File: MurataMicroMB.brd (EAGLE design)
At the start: 90 x 63 mm, 47 parts, among them CON1 C-2395.MurataMicroSD, CON3 CON_MIL_10_ARM, CON4 C-2395.microSD, IC1 74LVC1G00DBV, IC2 IC_DCDC_LM27313, IC3 IC_LPC11U3XQFN33, IC4 IC_LDO_XX1117_4, Q1 CLOCK_CRYSTAL_4_3225, SW1 SW_TACTSW_2PP8073, SW2 SW_TACTSW_2PP8073, SW3 SW_TACTSW_2PP8073, X1 TSW-102-02-S-S

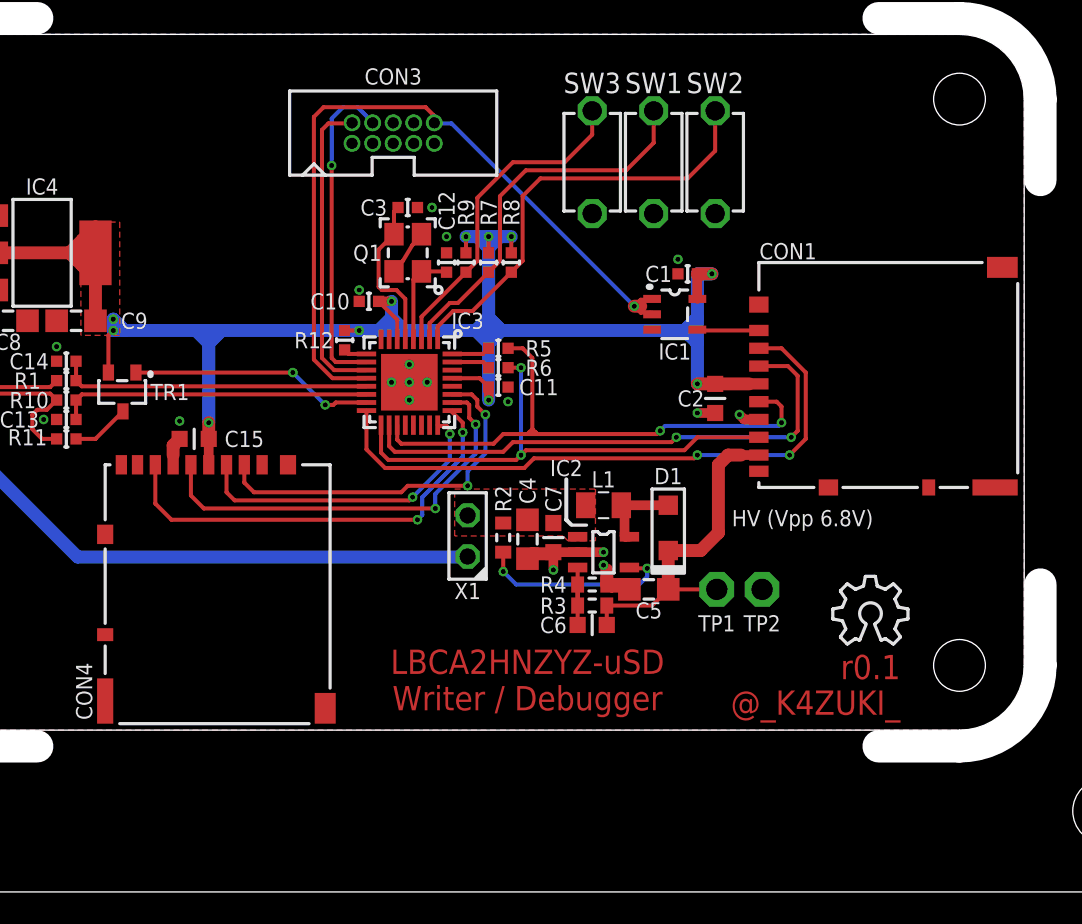
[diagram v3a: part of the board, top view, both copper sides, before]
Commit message: [ MB ][ SCH ] connection to uSD sockets changed
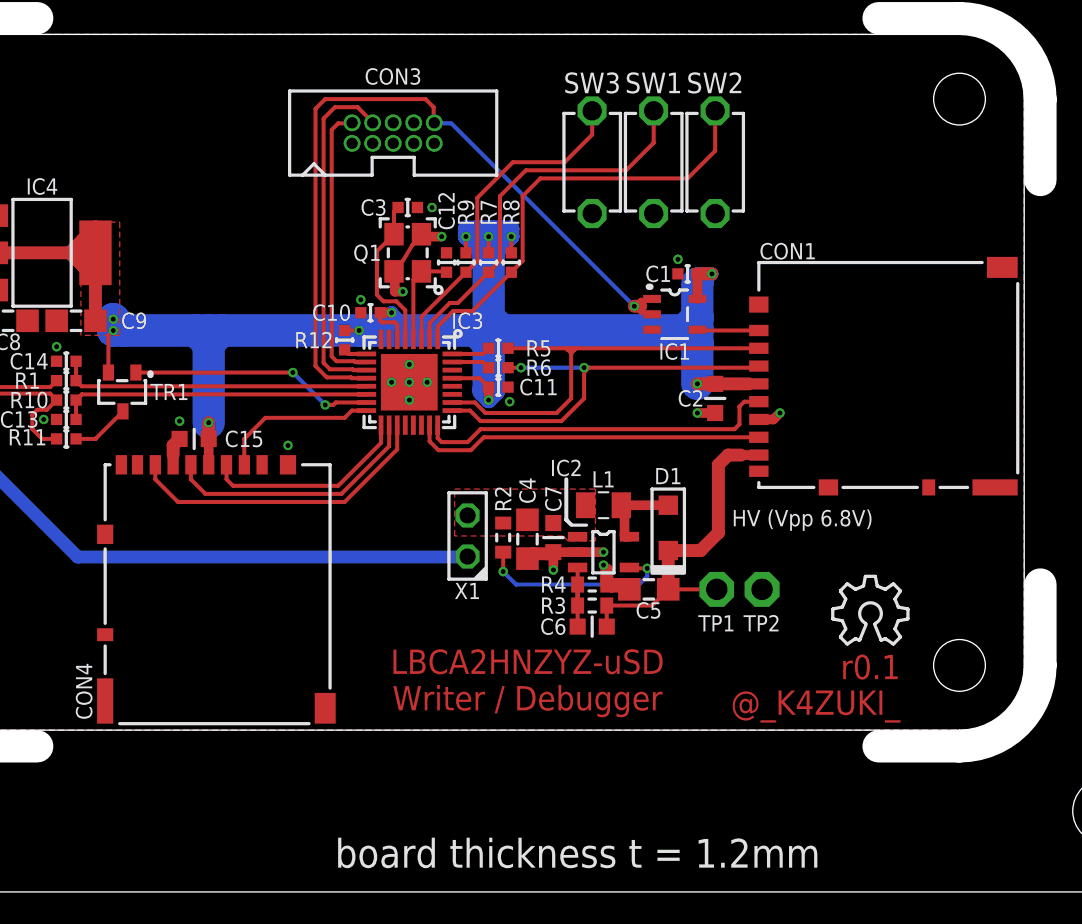
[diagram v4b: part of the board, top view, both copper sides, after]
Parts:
- moved C10 0.71 mm to (39.6, 35.8)
- moved C6 0.10 mm to (53.3, 16.4)
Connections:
- net !CS!: now also IC3.26, R5.2; no longer IC3.16
- net CS2: now also IC3.16; no longer IC3.27
- net MISO: now also IC3.23; no longer IC3.17, R6.2
- net MISO2: now also IC3.19; no longer IC3.25
- net MOSI: now also IC3.25, R6.2; no longer IC3.18
- net MOSI2: now also IC3.17; no longer IC3.24
- net SCK: now also IC3.24; no longer IC3.19, R5.2
- net SCK2: now also IC3.18; no longer IC3.26
- net SWCLK: now also IC3.11; no longer IC3.10
- net SWDIO: now also IC3.10; no longer IC3.11
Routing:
- net CS2: track 23.0 -> 9.87 mm, vias 2 -> 0
- net SCK: track 35.2 -> 22.4 mm, vias 2 -> 0
- net 3.3V: track 121.7 -> 133.4 mm
- net !CS!: track 38.4 -> 27.8 mm, vias 2 -> 0
- net MISO: track 32.0 -> 21.9 mm, vias 2 -> 0
- net SCK2: track 26.0 -> 16.0 mm, vias 2 -> 0
- net MISO2: track 27.2 -> 19.3 mm, vias 2 -> 0
- net MOSI2: track 19.5 -> 12.8 mm, vias 2 -> 0
- net MOSI: track 33.3 -> 26.9 mm
- net GND: track 16.9 -> 20.0 mm, vias 19 -> 21
- net SWDIO: track 19.2 -> 17.7 mm
- net SWCLK: track 20.3 -> 21.7 mm, vias 1 -> 0
- net NSRST: track 47.6 -> 48.7 mm
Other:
- board text added: "V-CUT"
- board text added: "board thickness t = 1.2mm"

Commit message: [ MB ] switches moved
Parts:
- moved SW1 3.80 mm to (60.9, 45.1)
- moved SW2 3.80 mm to (57.1, 45.1), turned to 270 degrees
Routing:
- net BL: track 27.3 -> 22.1 mm
- net !RESET!: track 23.8 -> 27.9 mm
- net 3.3V: track 133.4 -> 134.7 mm
- net GND: track 20.0 -> 21.2 mm
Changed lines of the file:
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@@
 <attribute name="VALUE" x="36.1" y="34.7" size="1" layer="27" font="vector" ratio="20" rot="R270"/>
 </element>
-<element name="SW1" library="mylib" package="SW_TACTSW_P8073" value="SW_TACTSW_2PP8073" x="57.1" y="45.1" smashed="yes" rot="R90">
+<element name="SW1" library="mylib" package="SW_TACTSW_P8073" value="SW_TACTSW_2PP8073" x="60.9" y="45.1" smashed="yes" rot="R90">
+<attribute name="NAME" x="60.9" y="50" size="1.27" layer="25" font="vector" ratio="16" rot="R180" align="center"/>
+<attribute name="VALUE" x="64.7" y="42.6" size="1.27" layer="27" font="vector" ratio="16" rot="R90"/>
+</element>
+<element name="SW2" library="mylib" package="SW_TACTSW_P8073" value="SW_TACTSW_2PP8073" x="57.1" y="45.1" smashed="yes" rot="R270">
 <attribute name="NAME" x="57.1" y="50" size="1.27" layer="25" font="vector" ratio="16" rot="R180" align="center"/>
-<attribute name="VALUE" x="60.9" y="42.6" size="1.27" layer="27" font="vector" ratio="16" rot="R90"/>
-</element>
-<element name="SW2" library="mylib" package="SW_TACTSW_P8073" value="SW_TACTSW_2PP8073" x="60.9" y="45.1" smashed="yes" rot="R90">
-<attribute name="NAME" x="60.9" y="50" size="1.27" layer="25" font="vector" ratio="16" align="center"/>
-<attribute name="VALUE" x="64.7" y="42.6" size="1.27" layer="27" font="vector" ratio="16" rot="R90"/>
+<attribute name="VALUE" x="53.3" y="47.6" size="1.27" layer="27" font="vector" ratio="16" rot="R270"/>
 </element>
 <element name="SW3" library="mylib" package="SW_TACTSW_P8073" value="SW_TACTSW_2PP8073" x="53.3" y="45.1" smashed="yes" rot="R90">
@@
 <wire x1="44" y1="40.5" x2="42.8" y2="40.5" width="0.6" layer="1"/>
 <wire x1="41" y1="38.3" x2="41.1" y2="38.3" width="0.6" layer="1"/>
+<wire x1="34.5" y1="27.6" x2="34.5" y2="26.4" width="0.8" layer="1"/>
 </signal>
 <signal name="D-">
@@
 <wire x1="36.7" y1="32.7" x2="37.1" y2="32.3" width="0.25" layer="1"/>
 <contactref element="IC3" pad="11"/>
-<wire x1="39.35" y1="32.25" x2="38.55" y2="32.25" width="0.25" layer="1"/>
-<wire x1="38.55" y1="32.25" x2="38.5" y2="32.3" width="0.25" layer="1"/>
-<wire x1="37.1" y1="32.3" x2="38.5" y2="32.3" width="0.25" layer="1"/>
+<wire x1="39.35" y1="32.25" x2="38.45" y2="32.25" width="0.25" layer="1"/>
+<wire x1="38.45" y1="32.25" x2="38.4" y2="32.3" width="0.25" layer="1"/>
+<wire x1="37.1" y1="32.3" x2="38.4" y2="32.3" width="0.25" layer="1"/>
 </signal>
 <signal name="SWDIO">
@@
 <wire x1="38.4" y1="47.5" x2="37.6" y2="47.5" width="0.25" layer="1"/>
 <contactref element="IC3" pad="10"/>
-<wire x1="39.35" y1="32.75" x2="38.65" y2="32.75" width="0.25" layer="1"/>
-<wire x1="38.65" y1="32.75" x2="38.6" y2="32.8" width="0.25" layer="1"/>
-<wire x1="37.5" y1="32.8" x2="38.6" y2="32.8" width="0.25" layer="1"/>
+<wire x1="39.35" y1="32.75" x2="38.55" y2="32.75" width="0.25" layer="1"/>
+<wire x1="38.55" y1="32.75" x2="38.5" y2="32.8" width="0.25" layer="1"/>
+<wire x1="37.5" y1="32.8" x2="38.5" y2="32.8" width="0.25" layer="1"/>
 </signal>
 <signal name="NSRST">
@@
 <wire x1="44.6" y1="47.5" x2="55.9" y2="36.2" width="0.25" layer="16"/>
 <contactref element="IC3" pad="12"/>
-<wire x1="39.35" y1="31.75" x2="38.45" y2="31.75" width="0.25" layer="1"/>
-<wire x1="38.45" y1="31.75" x2="38.4" y2="31.8" width="0.25" layer="1"/>
-<wire x1="36.9" y1="31.8" x2="38.4" y2="31.8" width="0.25" layer="1"/>
+<wire x1="39.35" y1="31.75" x2="38.35" y2="31.75" width="0.25" layer="1"/>
+<wire x1="38.35" y1="31.75" x2="38.3" y2="31.8" width="0.25" layer="1"/>
+<wire x1="36.9" y1="31.8" x2="38.3" y2="31.8" width="0.25" layer="1"/>
 </signal>
 <signal name="3.3V">
@@
 <wire x1="21.4" y1="39.9" x2="21.4" y2="39.1" width="0.8" layer="1"/>
 <wire x1="22.6" y1="37.9" x2="22.6" y2="35.3" width="0.8" layer="1"/>
-<wire x1="38" y1="34.7" x2="38.9" y2="34.7" width="0.25" layer="1"/>
-<via x="38.9" y="34.7" extent="1-16" drill="0.3"/>
+<wire x1="38" y1="34.7" x2="38.8" y2="34.7" width="0.25" layer="1"/>
+<via x="38.8" y="34.7" extent="1-16" drill="0.3"/>
 <via x="40.9" y="35.8" extent="1-16" drill="0.3"/>
 <wire x1="40.9" y1="35.8" x2="40.2" y2="35.8" width="0.6" layer="1"/>
 <polygon width="0.2" layer="1" thermals="no">
-<vertex x="21.7" y="34.4"/>
+<vertex x="21.7" y="33.7"/>
 <vertex x="21.7" y="41.4"/>
 <vertex x="24.1" y="41.4"/>
-<vertex x="24.1" y="34.4"/>
+<vertex x="24.1" y="33.7"/>
 </polygon>
-<via x="23.7" y="34.7" extent="1-16" drill="0.3"/>
-<via x="23.7" y="35.4" extent="1-16" drill="0.3"/>
+<via x="23.7" y="34.1" extent="1-16" drill="0.3"/>
+<via x="23.7" y="35.3" extent="1-16" drill="0.3"/>
 <wire x1="45.5" y1="39.5" x2="45.5" y2="40.5" width="0.25" layer="1"/>
 <via x="45.5" y="40.5" extent="1-16" drill="0.3"/>
@@
 <wire x1="46.9" y1="31.2" x2="46.9" y2="30.4" width="0.6" layer="1"/>
 <via x="46.9" y="30.4" extent="1-16" drill="0.3"/>
-<wire x1="23.7" y1="34.7" x2="23.7" y2="35.4" width="2" layer="16"/>
+<wire x1="23.7" y1="34.1" x2="23.7" y2="35.3" width="0.8" layer="16"/>
 <wire x1="24.4" y1="34.7" x2="28.8" y2="34.7" width="2" layer="16"/>
 <wire x1="28.8" y1="34.7" x2="29.6" y2="34.7" width="2" layer="16"/>
 <wire x1="29.6" y1="34.7" x2="30.4" y2="34.7" width="2" layer="16"/>
-<wire x1="30.4" y1="34.7" x2="38.9" y2="34.7" width="2" layer="16"/>
-<wire x1="23.7" y1="35.4" x2="24.4" y2="34.7" width="2" layer="16"/>
-<wire x1="38.9" y1="34.7" x2="40.9" y2="34.7" width="2" layer="16"/>
+<wire x1="30.4" y1="34.7" x2="38.8" y2="34.7" width="2" layer="16"/>
+<wire x1="23.7" y1="35.3" x2="24.4" y2="34.7" width="0.8" layer="16"/>
+<wire x1="38.8" y1="34.7" x2="40.9" y2="34.7" width="2" layer="16"/>
 <wire x1="40.9" y1="34.7" x2="46.1" y2="34.7" width="2" layer="16"/>
 <wire x1="46.1" y1="34.7" x2="46.9" y2="34.7" width="2" layer="16"/>
@@
 <wire x1="46.9" y1="35.5" x2="47.7" y2="34.7" width="2" layer="16"/>
 <wire x1="47.7" y1="34.7" x2="46.9" y2="33.9" width="2" layer="16"/>
-<wire x1="23.4" y1="34.4" x2="23.7" y2="34.7" width="0.25" layer="1"/>
+<wire x1="23.4" y1="33.8" x2="23.7" y2="34.1" width="0.25" layer="1"/>
 <via x="46.9" y="40.5" extent="1-16" drill="0.3"/>
-<wire x1="23.7" y1="34.7" x2="24.4" y2="34.7" width="2" layer="16"/>
-<wire x1="23.4" y1="32.1" x2="23.4" y2="34.4" width="0.25" layer="1"/>
+<wire x1="23.7" y1="34.1" x2="24.4" y2="34.7" width="0.8" layer="16"/>
+<wire x1="23.4" y1="32.1" x2="23.4" y2="33.8" width="0.25" layer="1"/>
 <contactref element="CON4" pad="VDD"/>
 <contactref element="C15" pad="1"/>
@@
 <wire x1="41.4" y1="35.3" x2="40.4" y2="35.3" width="0.8" layer="16"/>
 <wire x1="40.4" y1="35.3" x2="40.9" y2="35.8" width="0.8" layer="16"/>
+<wire x1="23.7" y1="35.3" x2="24.4" y2="35.3" width="0.8" layer="16"/>
+<wire x1="23.7" y1="34.1" x2="24.4" y2="34.1" width="0.8" layer="16"/>
 </signal>
 <signal name="N$3">
@@
 <contactref element="SW2" pad="A2"/>
 <wire x1="45.9" y1="35.9" x2="48.3" y2="38.3" width="0.25" layer="1"/>
-<wire x1="60.9" y1="48.275" x2="60.9" y2="45.8" width="0.25" layer="1"/>
-<wire x1="60.9" y1="45.8" x2="59.2" y2="44.1" width="0.25" layer="1"/>
 <wire x1="48.3" y1="38.3" x2="49" y2="39" width="0.25" layer="1"/>
 <wire x1="49" y1="39" x2="49" y2="43" width="0.25" layer="1"/>
-<wire x1="59.2" y1="44.1" x2="50.1" y2="44.1" width="0.25" layer="1"/>
+<wire x1="56.5" y1="44.1" x2="50.1" y2="44.1" width="0.25" layer="1"/>
 <wire x1="50.1" y1="44.1" x2="49" y2="43" width="0.25" layer="1"/>
+<wire x1="57.1" y1="41.925" x2="57.1" y2="43.5" width="0.25" layer="1"/>
+<wire x1="57.1" y1="43.5" x2="56.5" y2="44.1" width="0.25" layer="1"/>
 </signal>
 <signal name="!RESET!">
@@
 <wire x1="44.5" y1="36.4" x2="45" y2="36.4" width="0.25" layer="1"/>
 <contactref element="SW1" pad="A2"/>
-<wire x1="57.1" y1="48.275" x2="57.1" y2="46.3" width="0.25" layer="1"/>
-<wire x1="57.1" y1="46.3" x2="55.4" y2="44.6" width="0.25" layer="1"/>
 <wire x1="46.9" y1="38.3" x2="47.6" y2="39" width="0.25" layer="1"/>
 <wire x1="47.6" y1="39" x2="47.6" y2="43" width="0.25" layer="1"/>
-<wire x1="55.4" y1="44.6" x2="49.2" y2="44.6" width="0.25" layer="1"/>
+<wire x1="59.7" y1="44.6" x2="49.2" y2="44.6" width="0.25" layer="1"/>
 <wire x1="49.2" y1="44.6" x2="47.6" y2="43" width="0.25" layer="1"/>
+<wire x1="59.7" y1="44.6" x2="60.9" y2="45.8" width="0.25" layer="1"/>
+<wire x1="60.9" y1="45.8" x2="60.9" y2="48.275" width="0.25" layer="1"/>
 </signal>
 <signal name="N$5">
